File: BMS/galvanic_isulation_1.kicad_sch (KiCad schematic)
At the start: 12 parts

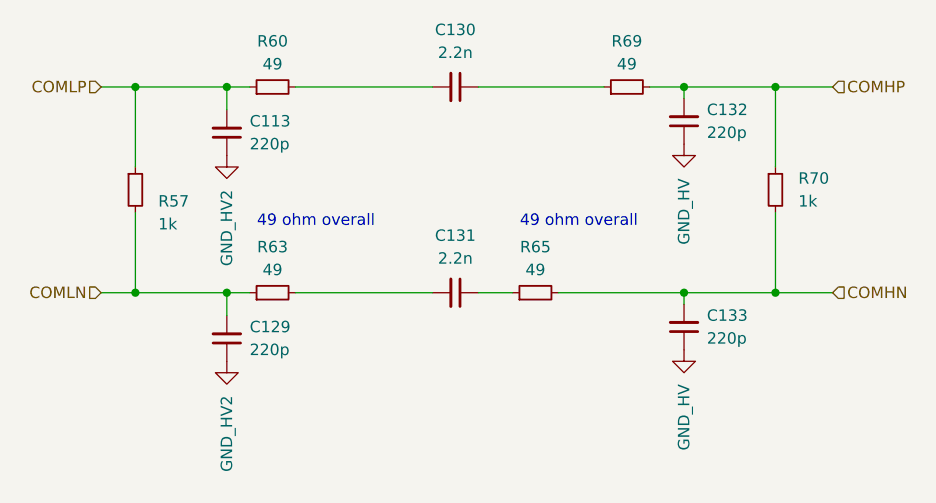
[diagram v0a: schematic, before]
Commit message: Dodano layout drugiego bq79614, ukladu tlumaczącego z protokułu TI na UART oraz wstępnie poprowadzono pary różnicowe
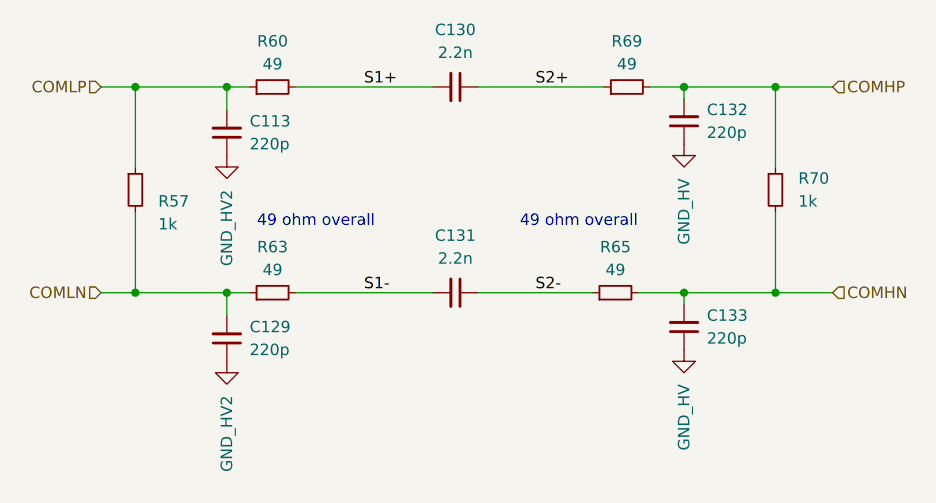
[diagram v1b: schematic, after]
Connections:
- net S2-: now reaches C131.1, R65.1
- net S1-: now reaches C131.2, R63.2
- net S1+: now reaches C130.2, R60.2
- net S2+: now reaches C130.1, R69.1
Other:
- moved on the sheet: R65
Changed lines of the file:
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@@
 	(wire
 		(pts
-			(xy 142.24 104.14) (xy 138.43 104.14)
+			(xy 151.13 104.14) (xy 138.43 104.14)
 		)
 		(stroke
@@
 	(wire
 		(pts
-			(xy 147.32 104.14) (xy 161.29 104.14)
+			(xy 156.21 104.14) (xy 161.29 104.14)
 		)
 		(stroke
@@
 				(size 1.27 1.27)
 			)
+		)
+	)
+	(label "S2-"
+		(at 144.78 104.14 0)
+		(fields_autoplaced yes)
+		(effects
+			(font
+				(size 1.27 1.27)
+			)
+			(justify left bottom)
+		)
+	)
+	(label "S1-"
+		(at 125.73 104.14 0)
+		(fields_autoplaced yes)
+		(effects
+			(font
+				(size 1.27 1.27)
+			)
+			(justify left bottom)
+		)
+	)
+	(label "S2+"
+		(at 144.78 81.28 0)
+		(fields_autoplaced yes)
+		(effects
+			(font
+				(size 1.27 1.27)
+			)
+			(justify left bottom)
+		)
+	)
+	(label "S1+"
+		(at 125.73 81.28 0)
+		(fields_autoplaced yes)
+		(effects
+			(font
+				(size 1.27 1.27)
+			)
+			(justify left bottom)
 		)
 	)
@@
 	(symbol
 		(lib_id "Device:R_Small")
-		(at 144.78 104.14 90)
+		(at 153.67 104.14 90)
 		(unit 1)
 		(exclude_from_sim no)
@@
 		(fields_autoplaced yes)
 		(property "Reference" "R65"
-			(at 144.78 99.06 90)
+			(at 153.67 99.06 90)
 			(effects
 				(font
@@
 		)
 		(property "Value" "49"
-			(at 144.78 101.6 90)
+			(at 153.67 101.6 90)
 			(effects
 				(font
@@
 		)
 		(property "Footprint" "Resistor_SMD:R_0603_1608Metric_Pad0.98x0.95mm_HandSolder"
-			(at 144.78 104.14 0)
+			(at 153.67 104.14 0)
 			(effects
 				(font
@@
 		)
 		(property "Datasheet" "https://www.mouser.pl/ProductDetail/KOA-Speer/RK73H1HRTTCM49R9F?qs=sGAEpiMZZMvdGkrng054txLI%2FDB4oIKDjd1z9Y%252BmyaXFChdzxTCbsQ%3D%3D"
-			(at 144.78 104.14 0)
+			(at 153.67 104.14 0)
 			(effects
 				(font
@@
 		)
 		(property "Description" "Resistor, small symbol"
-			(at 144.78 104.14 0)
-			(effects
-				(font
+			(at 153.67 104.14 0)
+			(effects
+				(font

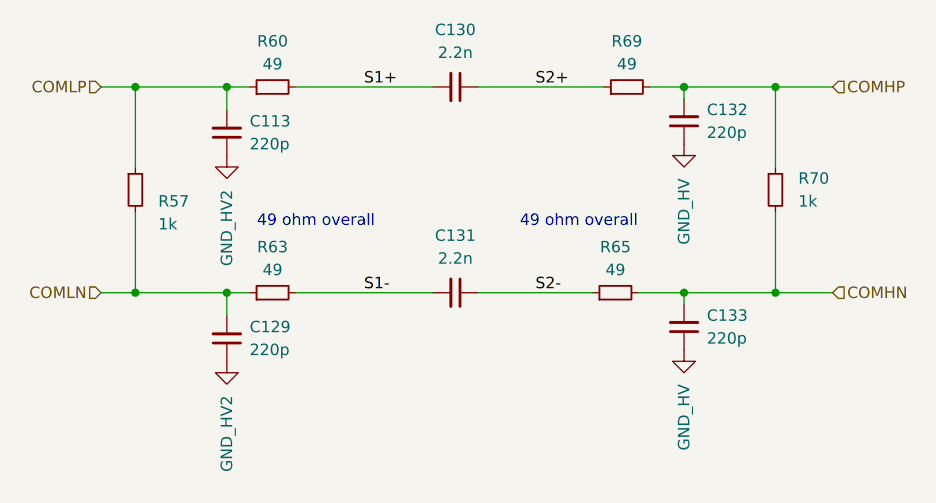
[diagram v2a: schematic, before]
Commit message: Zmienione kondensatory na kondensatory bezpieczeństwa,poprawiono strefy na thermal relief oraz naprawiono bledy z tym zwiazane, impedancja do zmiany jeszcze
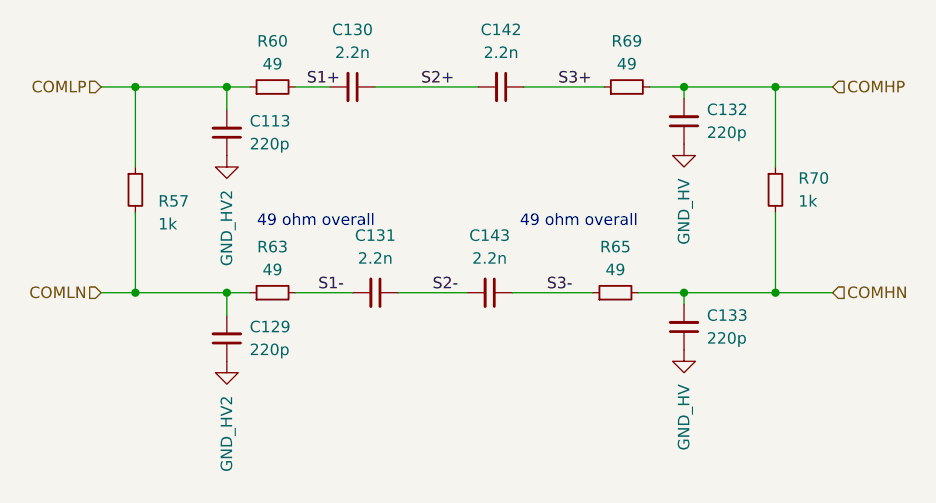
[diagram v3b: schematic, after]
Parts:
- added C142, C143: 2.2n, footrpint:CAPC5728X280N, symbol Device:C_Small
- C130, C131: footprint Capacitor_SMD:C_0603_1608Metric_Pad1.08x0.95mm_HandSolder -> footrpint:CAPC5728X280N
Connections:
- net S2+: now also C142.2; no longer R69.1
- net S2-: now also C143.2; no longer R65.1
- new net S3+: C142.1, R69.1
- new net S3-: C143.1, R65.1
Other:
- moved on the sheet: C130, C131
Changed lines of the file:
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@@
+	(wire
+		(pts
+			(xy 129.54 104.14) (xy 137.16 104.14)
+		)
+		(stroke
+			(width 0)
+			(type default)
+		)
+	)
 	(wire
 		(pts
@@
 	(wire
 		(pts
-			(xy 151.13 104.14) (xy 138.43 104.14)
-		)
-		(stroke
-			(width 0)
-			(type default)
-		)
-	)
-	(wire
-		(pts
-			(xy 138.43 81.28) (xy 152.4 81.28)
+			(xy 127 81.28) (xy 138.43 81.28)
+		)
+		(stroke
+			(width 0)
+			(type default)
+		)
+	)
+	(wire
+		(pts
+			(xy 142.24 104.14) (xy 151.13 104.14)
 		)
 		(stroke
@@
 	(wire
 		(pts
-			(xy 118.11 104.14) (xy 133.35 104.14)
+			(xy 118.11 104.14) (xy 124.46 104.14)
 		)
 		(stroke
@@
 	(wire
 		(pts
-			(xy 118.11 81.28) (xy 133.35 81.28)
+			(xy 118.11 81.28) (xy 121.92 81.28)
 		)
 		(stroke
@@
 	(wire
 		(pts
+			(xy 143.51 81.28) (xy 152.4 81.28)
+		)
+		(stroke
+			(width 0)
+			(type default)
+		)
+	)
+	(wire
+		(pts
 			(xy 96.52 81.28) (xy 100.33 81.28)
 		)
@@
 	)
 	(label "S2-"
-		(at 144.78 104.14 0)
+		(at 133.35 104.14 0)
 		(effects
 			(font
@@
 		)
 	)
-	(label "S1-"
-		(at 125.73 104.14 0)
+	(label "S3+"
+		(at 147.32 81.28 0)
 		(effects
 			(font
@@
 		)
 	)
-	(label "S2+"
-		(at 144.78 81.28 0)
+	(label "S1-"
+		(at 120.65 104.14 0)
 		(effects
 			(font
@@
 		)
 	)
+	(label "S3-"
+		(at 146.05 104.14 0)
+		(effects
+			(font
+				(size 1.27 1.27)
+			)
+			(justify left bottom)
+		)
+	)
+	(label "S2+"
+		(at 132.08 81.28 0)
+		(effects
+			(font
+				(size 1.27 1.27)
+			)
+			(justify left bottom)
+		)
+	)
 	(label "S1+"
-		(at 125.73 81.28 0)
+		(at 119.38 81.28 0)
 		(effects
 			(font
@@
 	)
 	(symbol
+		(lib_id "Device:C_Small")
+		(at 140.97 81.28 270)
+		(unit 1)
+		(exclude_from_sim no)
+		(in_bom yes)
+		(on_board yes)
+		(dnp no)
+		(fields_autoplaced yes)
+		(property "Reference" "C142"
+			(at 140.9636 74.93 90)
+			(effects
+				(font
+					(size 1.27 1.27)
+				)
+			)
+		)
+		(property "Value" "2.2n"
+			(at 140.9636 77.47 90)
+			(effects
+				(font
+					(size 1.27 1.27)
+				)
+			)
+		)
+		(property "Footprint" "footrpint:CAPC5728X280N"
+			(at 140.97 81.28 0)
+			(effects
+				(font
+					(size 1.27 1.27)
+				)
+				(hide yes)
+			)
+		)
+		(property "Datasheet" "https://www.mouser.pl/ProductDetail/Walsin/S252B222K502CT?qs=wUXugUrL1qx2Bha0j7hz5g%3D%3D"
+			(at 140.97 81.28 0)
+			(effects
+				(font
+					(size 1.27 1.27)
+				)
+				(hide yes)
+			)
+		)
+		(property "Description" "Kondensator Bezpieczeństwa 250V"
+			(at 140.97 81.28 0)
+			(effects
+				(font
+					(size 1.27 1.27)
+				)
+				(hide yes)
+			)
+		)
+		(pin "2"
+		)
+		(pin "1"
+		)
+		(instances
+			(project "BMS"
+				(path "/26289bb6-56bc-4ca1-b1a2-18d58d1afdf5/6e56498c-ea51-48f9-a89e-229056a470a5"
+					(reference "C142")
+					(unit 1)
+				)
+			)
+		)
+	)
+	(symbol
 		(lib_id "Device:R_Small")
 		(at 100.33 92.71 0)
@@
 	(symbol
 		(lib_id "Device:C_Small")
-		(at 135.89 104.14 270)
+		(at 127 104.14 270)
 		(unit 1)
 		(exclude_from_sim no)
@@
 		(fields_autoplaced yes)
 		(property "Reference" "C131"
-			(at 135.8836 97.79 90)
+			(at 126.9936 97.79 90)
 			(effects
 				(font
@@
 		)
 		(property "Value" "2.2n"
-			(at 135.8836 100.33 90)
-			(effects
-				(font
-					(size 1.27 1.27)
-				)
-			)
-		)
-		(property "Footprint" "Capacitor_SMD:C_0603_1608Metric_Pad1.08x0.95mm_HandSolder"
-			(at 135.89 104.14 0)
-			(effects
-				(font
-					(size 1.27 1.27)
-				)
-				(hide yes)
-			)
-		)
-		(property "Datasheet" "https://www.mouser.pl/ProductDetail/TDK/CGA3E2C0G1H222J080AE?qs=P1JMDcb91o5KNu2GzASXrQ%3D%3D"
-			(at 135.89 104.14 0)
-			(effects
-				(font
-					(size 1.27 1.27)
-				)
-				(hide yes)
-			)
-		)
-		(property "Description" "Unpolarized capacitor, small symbol"
-			(at 135.89 104.14 0)
+			(at 126.9936 100.33 90)
+			(effects
+				(font
+					(size 1.27 1.27)
+				)
+			)
+		)
+		(property "Footprint" "footrpint:CAPC5728X280N"
+			(at 127 104.14 0)
+			(effects
+				(font
+					(size 1.27 1.27)
+				)
+				(hide yes)
+			)
+		)
+		(property "Datasheet" "https://www.mouser.pl/ProductDetail/Walsin/S252B222K502CT?qs=wUXugUrL1qx2Bha0j7hz5g%3D%3D"
+			(at 127 104.14 0)
+			(effects
+				(font
+					(size 1.27 1.27)
+				)
+				(hide yes)
+			)
+		)
+		(property "Description" "Kondensator Bezpieczeństwa 250V"
+			(at 127 104.14 0)
 			(effects
 				(font
@@
 	)
 	(symbol
+		(lib_id "Device:C_Small")
+		(at 139.7 104.14 270)
+		(unit 1)
+		(exclude_from_sim no)
+		(in_bom yes)
+		(on_board yes)
+		(dnp no)
+		(fields_autoplaced yes)
+		(property "Reference" "C143"
+			(at 139.6936 97.79 90)
+			(effects
+				(font
+					(size 1.27 1.27)
+				)
+			)
+		)
+		(property "Value" "2.2n"
+			(at 139.6936 100.33 90)
+			(effects
+				(font
+					(size 1.27 1.27)
+				)
+			)
+		)
+		(property "Footprint" "footrpint:CAPC5728X280N"
+			(at 139.7 104.14 0)
+			(effects
+				(font
+					(size 1.27 1.27)
+				)
+				(hide yes)
+			)
+		)
+		(property "Datasheet" "https://www.mouser.pl/ProductDetail/Walsin/S252B222K502CT?qs=wUXugUrL1qx2Bha0j7hz5g%3D%3D"
+			(at 139.7 104.14 0)
+			(effects
+				(font
+					(size 1.27 1.27)
+				)
+				(hide yes)
+			)
+		)
+		(property "Description" "Kondensator Bezpieczeństwa 250V"
+			(at 139.7 104.14 0)
+			(effects
+				(font
+					(size 1.27 1.27)
+				)
+				(hide yes)
+			)
+		)
+		(pin "2"
+		)
+		(pin "1"
+		)
+		(instances
+			(project "BMS"
+				(path "/26289bb6-56bc-4ca1-b1a2-18d58d1afdf5/6e56498c-ea51-48f9-a89e-229056a470a5"
+					(reference "C143")
+					(unit 1)
+				)
+			)
+		)
+	)
+	(symbol
 		(lib_id "Device:R_Small")
 		(at 171.45 92.71 0)
@@
 	(symbol
 		(lib_id "Device:C_Small")
-		(at 135.89 81.28 270)
+		(at 124.46 81.28 270)
 		(unit 1)
 		(exclude_from_sim no)
@@
 		(fields_autoplaced yes)
 		(property "Reference" "C130"
-			(at 135.8836 74.93 90)
+			(at 124.4536 74.93 90)
 			(effects
 				(font
@@
 		)
 		(property "Value" "2.2n"
-			(at 135.8836 77.47 90)
-			(effects
-				(font
-					(size 1.27 1.27)
-				)
-			)
-		)
-		(property "Footprint" "Capacitor_SMD:C_0603_1608Metric_Pad1.08x0.95mm_HandSolder"
-			(at 135.89 81.28 0)
-			(effects
-				(font
-					(size 1.27 1.27)
-				)
-				(hide yes)
-			)
-		)
-		(property "Datasheet" "https://www.mouser.pl/ProductDetail/TDK/CGA3E2C0G1H222J080AE?qs=P1JMDcb91o5KNu2GzASXrQ%3D%3D"
-			(at 135.89 81.28 0)
-			(effects
-				(font
-					(size 1.27 1.27)
-				)
-				(hide yes)
-			)
-		)
-		(property "Description" "Unpolarized capacitor, small symbol"
-			(at 135.89 81.28 0)
-			(effects
-				(font
+			(at 124.4536 77.47 90)
+			(effects
+				(font
+					(size 1.27 1.27)
+				)
+			)
+		)
+		(property "Footprint" "footrpint:CAPC5728X280N"
+			(at 124.46 81.28 0)
+			(effects
+				(font
+					(size 1.27 1.27)
+				)
+				(hide yes)
+			)
+		)
+		(property "Datasheet" "https://www.mouser.pl/ProductDetail/Walsin/S252B222K502CT?qs=wUXugUrL1qx2Bha0j7hz5g%3D%3D"
+			(at 124.46 81.28 0)
+			(effects
+				(font
+					(size 1.27 1.27)
+				)
+				(hide yes)
+			)
+		)
+		(property "Description" "Kondensator Bezpieczeństwa 250V"
+			(at 124.46 81.28 0)
+			(effects
+				(font
